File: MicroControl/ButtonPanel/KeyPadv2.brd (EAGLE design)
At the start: 59 x 109.8 mm, 27 parts, among them SW1 SW-12-12, SW10 SW-12-12, SW11 SW-12-12, SW12 SW-12-12, SW2 SW-12-12, SW3 SW-12-12, SW4 SW-12-12, SW5 SW-12-12, SW6 SW-12-12, SW7 SW-12-12, SW8 SW-12-12, SW9 SW-12-12

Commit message: что-то ошло не так
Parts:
- flipped U$2 to the bottom
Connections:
- net COL1: now also U$2.10; no longer U$2.9
- net COL2: now also U$2.9; no longer U$2.10
- net COL3: now also U$2.8; no longer U$2.16
- net ENC-COM: now also U$2.20/A2; no longer U$2.3
- net ENC1: now also U$2.21/A3; no longer U$2.2
- net ENC2: now also U$2.19/A1; no longer U$2.4
- net MOD1: now also U$2.2; no longer U$2.21/A3
- net MOD2: now also U$2.3; no longer U$2.20/A2
- net MOD3: now also U$2.4; no longer U$2.19/A1
- net MOD4: now also U$2.5; no longer U$2.18/A0
- net ROW1: now also U$2.6; no longer U$2.15
- net ROW2: now also U$2.16; no longer U$2.8
- net ROW3: now also U$2.14; no longer U$2.7
- net ROW4: now also U$2.15; no longer U$2.6
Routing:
- net GND: track 113.3 -> 117.4 mm
- net COL1: track 62.9 -> 61.1 mm
- net COL2: track 95.3 -> 94.7 mm

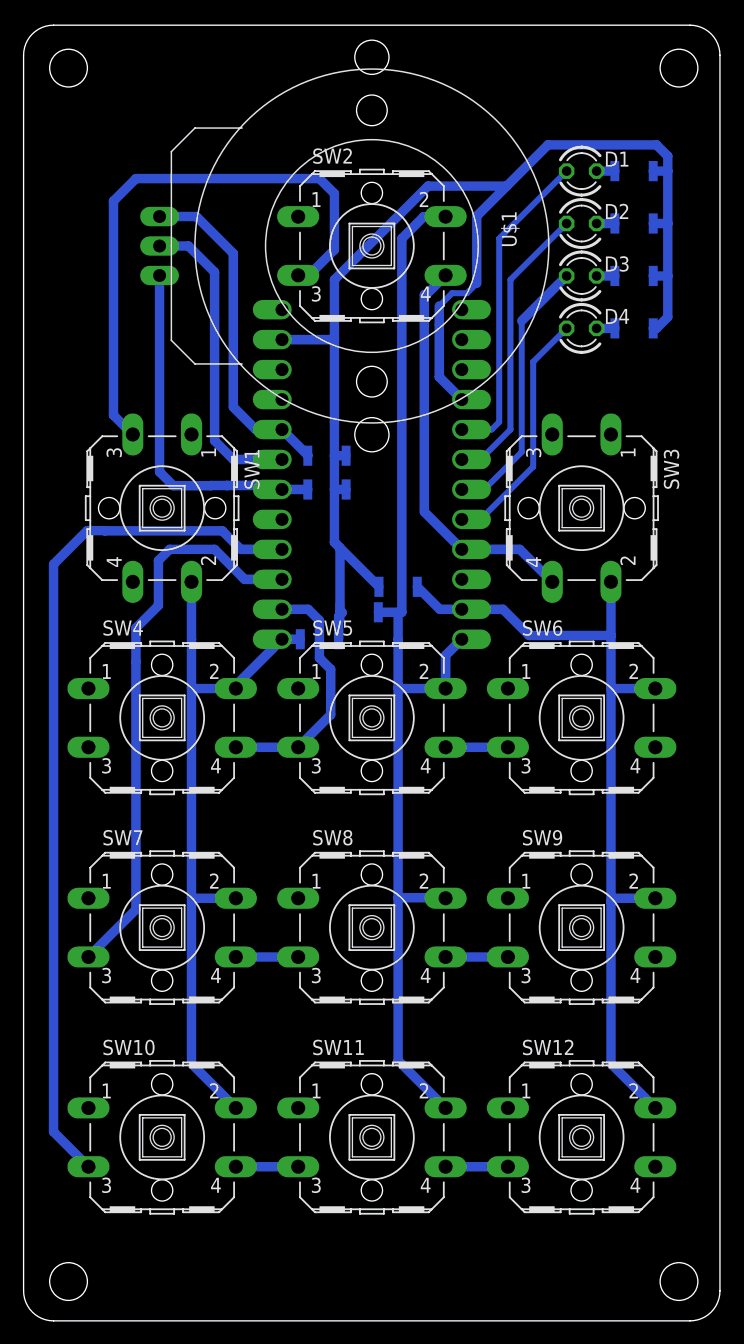
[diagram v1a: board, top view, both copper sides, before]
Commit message: Выносной USB
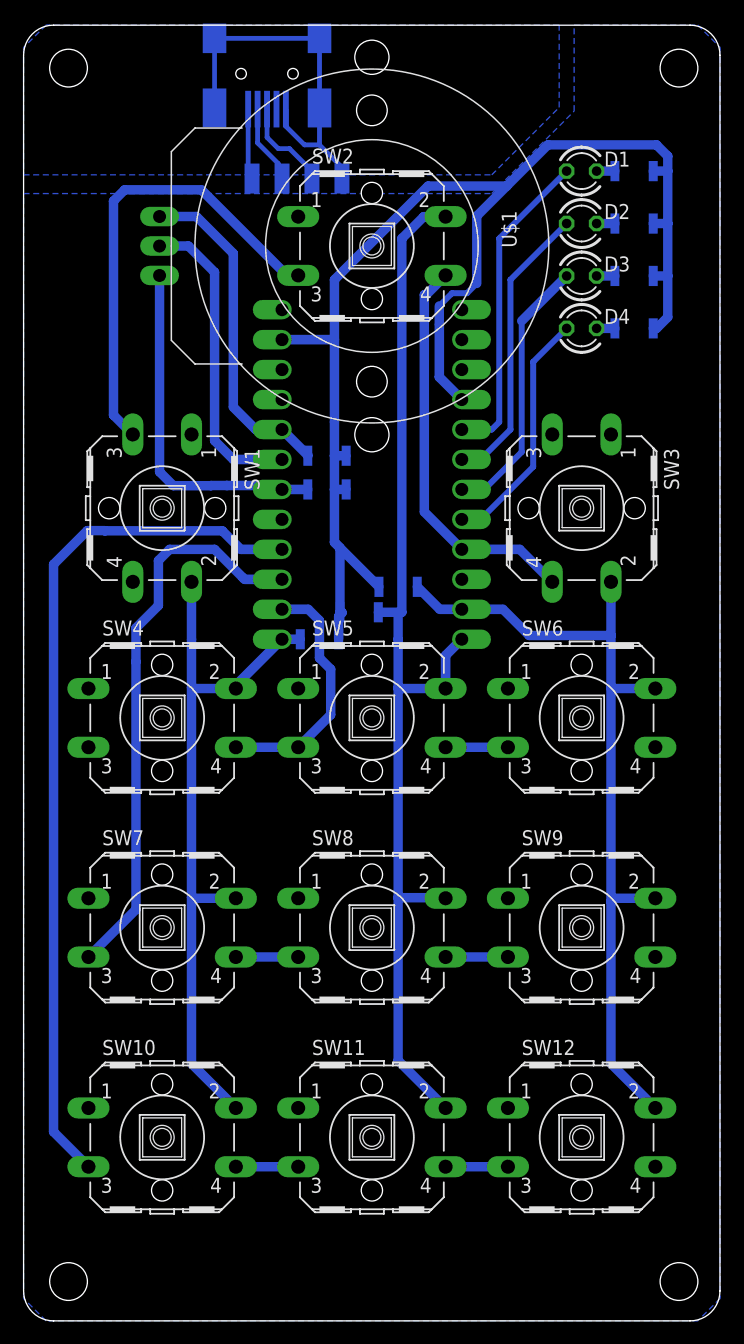
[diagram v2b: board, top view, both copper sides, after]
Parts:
- added D+, D-, G, V: (no value), wirepad:SMD1,27-2,54
- added X1: USB-MINIMICROMINI-SMD1, Flamberm:32005-201
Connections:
- new net D+: D+.1, X1.3
- new net D-: D-.1, X1.2
- new net G: G.1, X1.5, X1.M1, X1.M2, X1.M3, X1.M4
- new net V: V.1, X1.1
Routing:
- net G: track 0.00 -> 32.4 mm
- net ROW1: track 83.4 -> 73.7 mm
- net D+: track 0.00 -> 8.03 mm
- net D-: track 0.00 -> 6.75 mm
- net V: track 0.00 -> 6.03 mm
- added copper zone on layer 16, net G
- added copper zone on layer 16, net GND
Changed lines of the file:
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@@
 </layers>
 <board>
-<fusionsync huburn="a.cGVyc29uYWw6dWUyOGRlMGUz" projecturn="a.cGVyc29uYWw6dWUyOGRlMGUzIzIwMTcwNDA2NzA3MTU3MDY" f3durn="urn:adsk.wipprod:dm.lineage:9VDeFdeySWCQg1oP2-vJOQ" pcbguid="80d599bc-69fc-4b5d-a1f4-8936e177376f" lastpulledtime="" lastsyncedchangeguid="61306478-a65d-cfb7-8779-96732d88a768"/>
+<fusionsync huburn="a.cGVyc29uYWw6dWUyOGRlMGUz" projecturn="a.cGVyc29uYWw6dWUyOGRlMGUzIzIwMTcwNDA2NzA3MTU3MDY" f3durn="urn:adsk.wipprod:dm.lineage:9VDeFdeySWCQg1oP2-vJOQ" pcbguid="80d599bc-69fc-4b5d-a1f4-8936e177376f" lastpulledtime="" lastsyncedchangeguid="b3d9f99c-a314-64fc-83dd-2c5f096886fc"/>
 <plain>
 <wire x1="59.035" y1="3.175" x2="59.035" y2="107.9375" width="0" layer="20"/>
@@
 <element name="D3" library="Flamberm" library_urn="urn:adsk.eagle:library:2654185" package="LED3MM" package3d_urn="urn:adsk.eagle:package:2654616/2" value="LED_3MM" x="47.3075" y="89.2175"/>
 <element name="D4" library="Flamberm" library_urn="urn:adsk.eagle:library:2654185" package="LED3MM" package3d_urn="urn:adsk.eagle:package:2654616/2" value="LED_3MM" x="47.3075" y="84.7725"/>
+<element name="X1" library="Flamberm" library_urn="urn:adsk.eagle:library:2654185" package="32005-201" package3d_urn="urn:adsk.eagle:package:2654593/1" value="USB-MINIMICROMINI-SMD1" x="20.6375" y="106.3625" rot="MR270">
+<attribute name="MF" value="" x="20.6375" y="106.3625" size="1.778" layer="28" rot="MR270" display="off"/>
+<attribute name="MPN" value="" x="20.6375" y="106.3625" size="1.778" layer="28" rot="MR270" display="off"/>
+<attribute name="OC_FARNELL" value="unknown" x="20.6375" y="106.3625" size="1.778" layer="28" rot="MR270" display="off"/>
+<attribute name="OC_NEWARK" value="unknown" x="20.6375" y="106.3625" size="1.778" layer="28" rot="MR270" display="off"/>
+</element>
+<element name="V" library="wirepad" library_urn="urn:adsk.eagle:library:412" package="SMD1,27-2,54" package3d_urn="urn:adsk.eagle:package:30839/1" value="" x="19.3675" y="97.4725" rot="MR180"/>
+<element name="D-" library="wirepad" library_urn="urn:adsk.eagle:library:412" package="SMD1,27-2,54" package3d_urn="urn:adsk.eagle:package:30839/1" value="" x="21.9075" y="97.4725" rot="MR180"/>
+<element name="D+" library="wirepad" library_urn="urn:adsk.eagle:library:412" package="SMD1,27-2,54" package3d_urn="urn:adsk.eagle:package:30839/1" value="" x="24.4475" y="97.4725" rot="MR180"/>
+<element name="G" library="wirepad" library_urn="urn:adsk.eagle:library:412" package="SMD1,27-2,54" package3d_urn="urn:adsk.eagle:package:30839/1" value="" x="26.9875" y="97.4725" rot="MR180"/>
 </elements>
 <signals>
@@
 <wire x1="35.2425" y1="80.645" x2="37.1475" y2="78.74" width="0.8128" layer="16"/>
 <wire x1="26.3525" y1="83.82" x2="21.9075" y2="83.82" width="0.8128" layer="16"/>
+<polygon width="0.4064" layer="16" isolate="0.6096" orphans="yes">
+<vertex x="0" y="96.2025"/>
+<vertex x="39.6875" y="96.2025"/>
+<vertex x="46.6725" y="103.1875"/>
+<vertex x="46.6725" y="110.49"/>
+<vertex x="57.15" y="110.49"/>
+<vertex x="59.055" y="108.585"/>
+<vertex x="59.055" y="2.54"/>
+<vertex x="57.15" y="0.635"/>
+<vertex x="1.905" y="0.635"/>
+<vertex x="0" y="2.54"/>
+</polygon>
 </signal>
 <signal name="0">
@@
 <wire x1="34.1376" y1="87.63" x2="33.9725" y2="87.63" width="0.8" layer="16"/>
 <wire x1="33.9725" y1="87.63" x2="33.9725" y2="69.215" width="0.8" layer="16"/>
-<wire x1="23.2791" y1="89.2683" x2="24.1808" y2="89.2683" width="0.8" layer="16"/>
-<wire x1="24.1808" y1="89.2683" x2="26.3525" y2="91.44" width="0.8" layer="16"/>
-<wire x1="26.3525" y1="91.44" x2="26.3525" y2="96.2025" width="0.8" layer="16"/>
-<wire x1="26.3525" y1="96.2025" x2="25.0825" y2="97.4725" width="0.8" layer="16"/>
-<wire x1="25.0825" y1="97.4725" x2="9.525" y2="97.4725" width="0.8" layer="16"/>
-<wire x1="9.525" y1="97.4725" x2="7.62" y2="95.5675" width="0.8" layer="16"/>
+<wire x1="15.0749" y1="96.52" x2="8.5725" y2="96.52" width="0.8" layer="16"/>
+<wire x1="8.5725" y1="96.52" x2="7.62" y2="95.5675" width="0.8" layer="16"/>
 <wire x1="7.62" y1="95.5675" x2="7.62" y2="77.4192" width="0.8" layer="16"/>
 <wire x1="7.62" y1="77.4192" x2="9.2583" y2="75.7809" width="0.8" layer="16"/>
@@
 <wire x1="42.0624" y1="66.04" x2="37.1475" y2="66.04" width="0.8128" layer="16"/>
 <wire x1="33.9725" y1="69.215" x2="37.1475" y2="66.04" width="0.8128" layer="16"/>
+<wire x1="22.3266" y1="89.2683" x2="15.0749" y2="96.52" width="0.8128" layer="16"/>
+<wire x1="23.2791" y1="89.2683" x2="22.3266" y2="89.2683" width="0.8128" layer="16"/>
 </signal>
 <signal name="ROW4">
@@
 <contactref element="U$2" pad="VCC"/>
 </signal>
+<signal name="V">
+<contactref element="X1" pad="1"/>
+<contactref element="V" pad="1"/>
+<wire x1="19.0375" y1="103.3625" x2="19.0375" y2="97.8025" width="0.4064" layer="16"/>
+<wire x1="19.0375" y1="97.8025" x2="19.3675" y2="97.4725" width="0.4064" layer="16"/>
+</signal>
+<signal name="D-">
+<contactref element="X1" pad="2"/>
+<contactref element="D-" pad="1"/>
+<wire x1="19.8375" y1="103.3625" x2="19.8375" y2="100.495" width="0.4064" layer="16"/>
+<wire x1="19.8375" y1="100.495" x2="21.59" y2="98.7425" width="0.4064" layer="16"/>
+<wire x1="21.59" y1="98.7425" x2="21.59" y2="97.79" width="0.4064" layer="16"/>
+<wire x1="21.59" y1="97.79" x2="21.9075" y2="97.4725" width="0.4064" layer="16"/>
+</signal>
+<signal name="D+">
+<contactref element="X1" pad="3"/>
+<contactref element="D+" pad="1"/>
+<wire x1="20.6375" y1="103.3625" x2="20.6375" y2="100.965" width="0.4064" layer="16"/>
+<wire x1="20.6375" y1="100.965" x2="21.59" y2="100.0125" width="0.4064" layer="16"/>
+<wire x1="21.59" y1="100.0125" x2="22.5425" y2="100.0125" width="0.4064" layer="16"/>
+<wire x1="22.5425" y1="100.0125" x2="24.4475" y2="98.1075" width="0.4064" layer="16"/>
+<wire x1="24.4475" y1="98.1075" x2="24.4475" y2="97.4725" width="0.4064" layer="16"/>
+</signal>
+<signal name="G">
+<contactref element="X1" pad="5"/>
+<contactref element="G" pad="1"/>
+<wire x1="22.2375" y1="103.3625" x2="22.2375" y2="101.905" width="0.4064" layer="16"/>
+<wire x1="22.2375" y1="101.905" x2="23.8125" y2="100.33" width="0.4064" layer="16"/>
+<wire x1="23.8125" y1="100.33" x2="25.0825" y2="100.33" width="0.4064" layer="16"/>
+<wire x1="25.0825" y1="100.33" x2="26.9875" y2="98.425" width="0.4064" layer="16"/>
+<wire x1="26.9875" y1="98.425" x2="26.9875" y2="97.4725" width="0.4064" layer="16"/>
+<contactref element="X1" pad="M4"/>
+<contactref element="X1" pad="M3"/>
+<contactref element="X1" pad="M1"/>
+<contactref element="X1" pad="M2"/>
+<wire x1="25.0875" y1="103.4625" x2="25.0875" y2="100.335" width="0.4064" layer="16"/>
+<wire x1="25.0875" y1="100.335" x2="25.0825" y2="100.33" width="0.4064" layer="16"/>
+<wire x1="25.0875" y1="109.3625" x2="25.0875" y2="103.4625" width="0.4064" layer="16"/>
+<wire x1="16.1875" y1="109.3625" x2="16.1875" y2="103.4625" width="0.4064" layer="16"/>
+<wire x1="25.0875" y1="109.3625" x2="16.1875" y2="109.3625" width="0.4064" layer="16"/>
+<polygon width="0.4064" layer="16" isolate="0.6096">
+<vertex x="0" y="97.79"/>
+<vertex x="39.6875" y="97.79"/>
+<vertex x="45.4025" y="103.505"/>
+<vertex x="45.4025" y="110.49"/>
+<vertex x="1.905" y="110.49"/>
+<vertex x="0" y="108.585"/>
+</polygon>
+</signal>
 </signals>
